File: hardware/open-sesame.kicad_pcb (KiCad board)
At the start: 2 copper layers, 72 x 45 mm, 33 parts, among them J1 Conn_01x02, J2 Conn_01x06, J3 Conn_01x02, J4 Conn_01x02, J5 Conn_01x02, J6 Conn_01x02, J7 Qwiic_RA, U1 CPC1019N, U2 CPC1019N, U3 CPC1019N

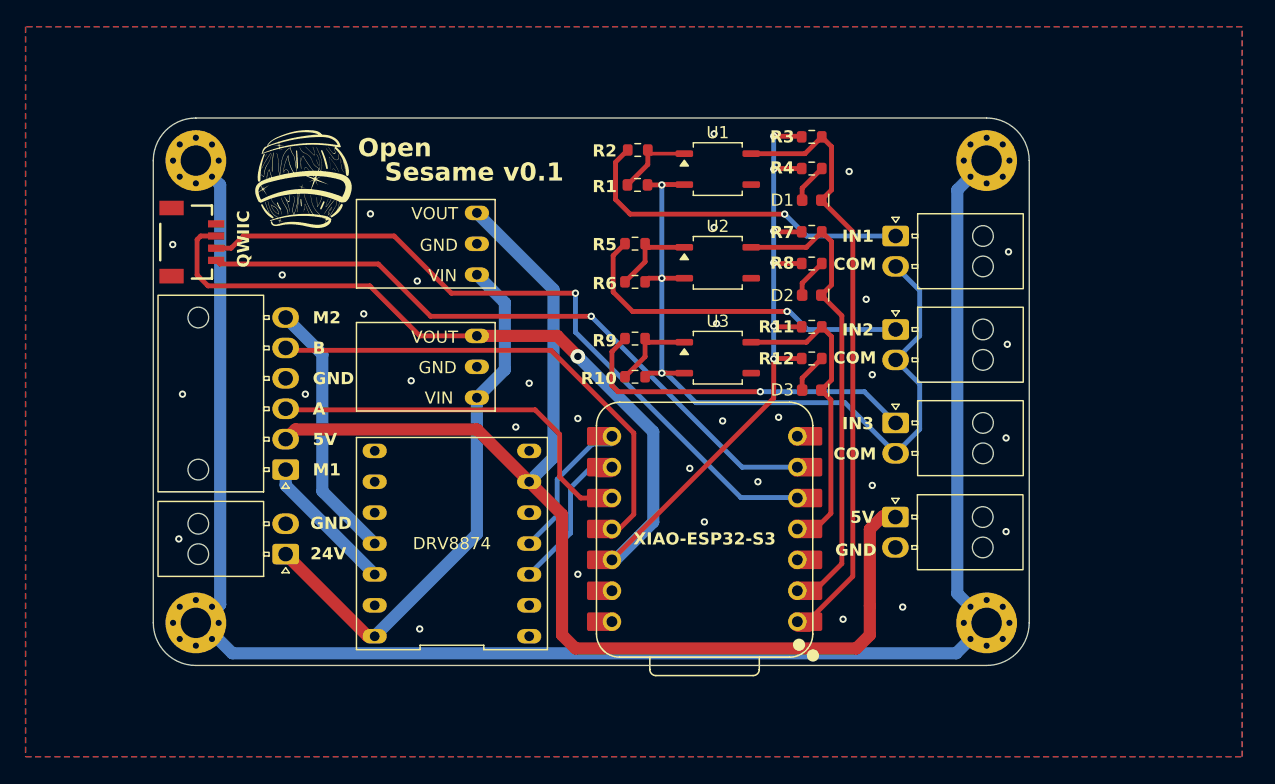
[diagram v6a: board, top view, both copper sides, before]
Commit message: hardware: Use screw connectors and PC817
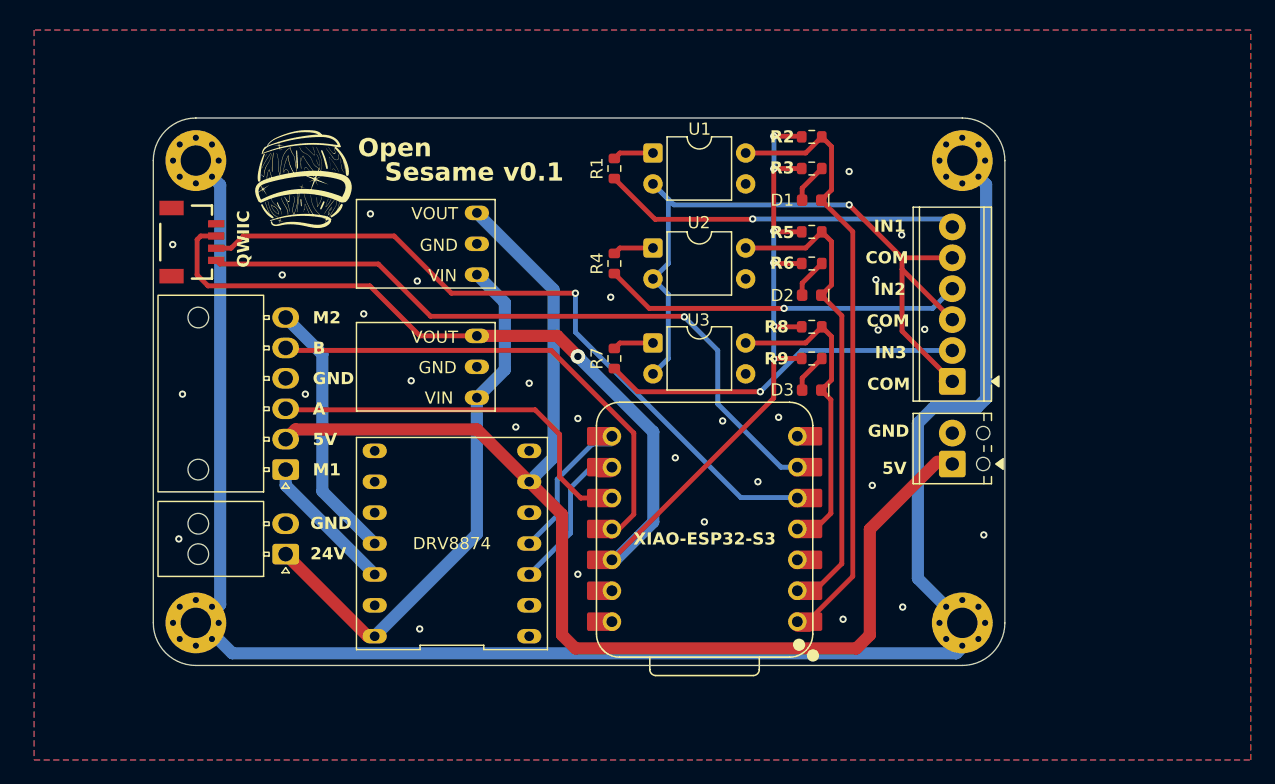
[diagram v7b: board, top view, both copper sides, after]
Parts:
- removed J5, J6: Conn_01x02, Connector_Molex:Molex_Nano-Fit_105313-xx02_1x02_P2.50mm_Horizontal
- removed R10: 750R, Resistor_SMD:R_0603_1608Metric
- removed the R2 at (160.3, 70.1)
- removed the R5 at (160.1, 77.8)
- removed the R6 at (160.1, 81.0)
- removed the R9 at (160.1, 85.6)
- added R4: 330R, Resistor_SMD:R_0603_1608Metric, F.Cu at (158.4, 79.5)
- added R7: 330R, Resistor_SMD:R_0603_1608Metric, F.Cu at (158.4, 87.3)
- J3: value Conn_01x02 -> Screw_Terminal_01x02; footprint Connector_Molex:Molex_Nano-Fit_105313-xx02_1x02_P2.50mm_Horizontal -> TerminalBlock_Phoenix:TerminalBlock_Phoenix_MPT-0,5-2-2.54_1x02_P2.54mm_Horizontal
- J4: value Conn_01x02 -> Screw_Terminal_01x06; footprint Connector_Molex:Molex_Nano-Fit_105313-xx02_1x02_P2.50mm_Horizontal -> TerminalBlock_Phoenix:TerminalBlock_Phoenix_MPT-0,5-6-2.54_1x06_P2.54mm_Horizontal
- R1: value 750R -> 330R
- U1, U2, U3: value CPC1019N -> PC817; footprint Package_SO:SOP-4_3.8x4.1mm_P2.54mm -> Package_DIP:DIP-4_W7.62mm
- moved J4 12.8 mm to (186.2, 89.2), turned to 90 degrees
- moved J3 6.40 mm to (186.2, 95.9), turned to 90 degrees
- moved U1 5.49 mm to (161.6, 70.4)
- moved U2 5.46 mm to (161.6, 78.2)
- moved U3 5.46 mm to (161.6, 86.0)
- moved R1 2.33 mm to (158.4, 71.7), turned to 90 degrees
- moved H1 2.00 mm to (187.0, 71.0)
- moved H2 2.00 mm to (187.0, 109.0)
- renumbered R3 to R2, R4 to R3, R7 to R5, R8 to R6, R11 to R8, R12 to R9
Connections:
- J4 pad 1: IN1 -> IN_COMMON
- J4 pad 2: IN_COMMON -> IN3
- R1 pad 1: Net-(R1-Pad1) -> IN1
- R1 pad 2: IN_COMMON -> Net-(R1-Pad2)
- U1 pad 1: Net-(R1-Pad1) -> Net-(R1-Pad2)
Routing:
- net Net-(R1-Pad1): track 6.69 -> 0.00 mm
- net +5V: track 98.9 -> 104.2 mm
- net Earth: track 146.0 -> 150.8 mm
- net Net-(R7-Pad2): track 7.17 -> 3.36 mm
- net Net-(R4-Pad2): track 7.17 -> 3.36 mm
- net Net-(R1-Pad2): track 0.00 -> 3.36 mm
- net SCL: track 54.8 -> 57.4 mm
- net IN_COMMON: track 65.8 -> 63.5 mm, vias 3 -> 1
- net IN3: track 28.9 -> 30.0 mm
- net IN2: track 28.9 -> 29.6 mm
- net IN1: track 28.7 -> 29.5 mm
- net GND: vias 32 -> 29
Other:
- board size 72 x 45 mm -> 70 x 45 mm

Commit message: hardware: use one power converter, shrink size, change connectors
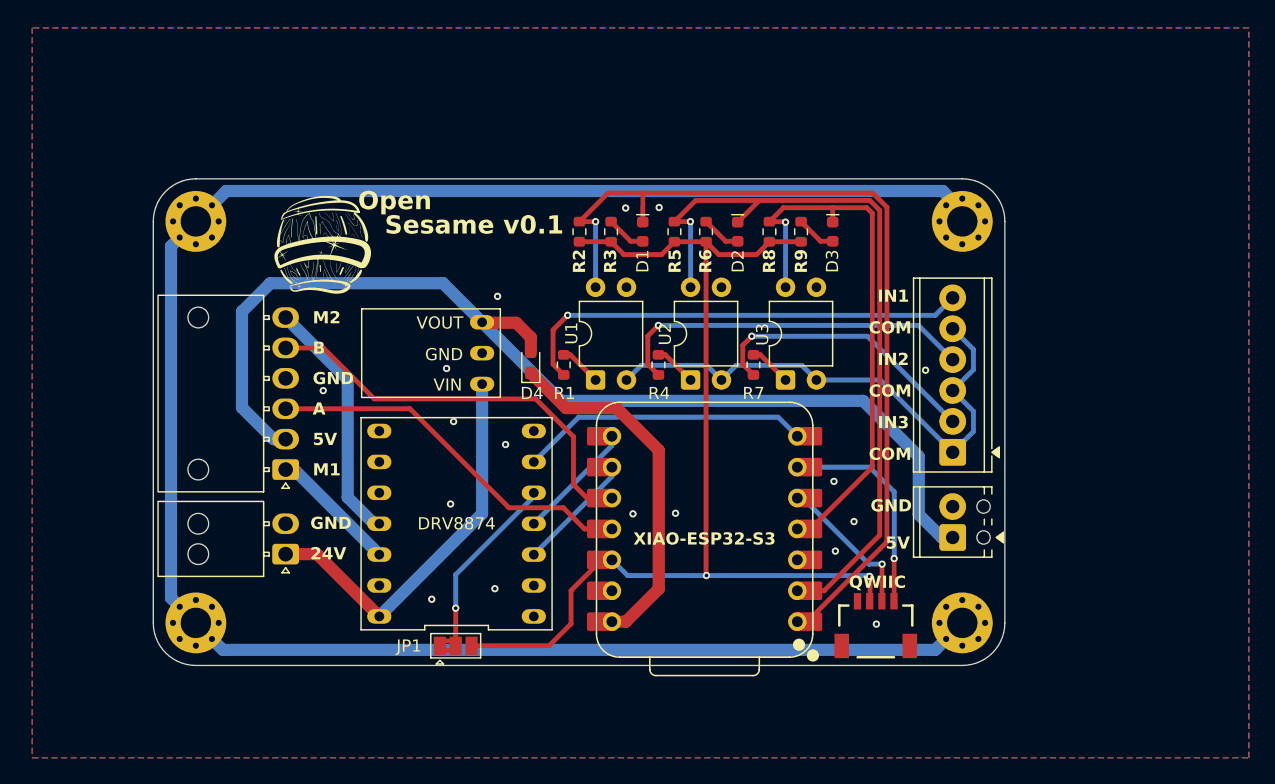
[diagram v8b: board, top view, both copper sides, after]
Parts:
- removed D45V5F2: D45V5F3, MyLibrary:D45V5Fx
- added D4: D_Schottky, Diode_SMD:D_0603_1608Metric_Pad1.05x0.95mm_HandSolder, F.Cu at (151.5, 87.6)
- added JP1: SolderJumper_3_Bridged12, Jumper:SolderJumper-3_P1.3mm_Bridged2Bar12_Pad1.0x1.5mm, F.Cu at (145.4, 110.9)
- moved J7 61.7 mm to (179.9, 107.2), turned to 0 degrees
- moved R2 20.6 mm to (155.5, 76.8), turned to 90 degrees
- moved U1 19.2 mm to (156.9, 89.0), turned to 90 degrees
- moved R3 17.3 mm to (158.1, 76.8), turned to 90 degrees
- moved R1 16.7 mm to (154.2, 87.8)
- moved D1 14.1 mm to (160.7, 76.8), turned to -90 degrees
- moved D3 13.1 mm to (176.3, 76.8), turned to -90 degrees
- moved R7 11.4 mm to (169.8, 87.8)
- moved U3 11.3 mm to (172.5, 89.0), turned to 90 degrees
- moved R5 11.3 mm to (163.3, 76.8), turned to 90 degrees
- moved U2 11.3 mm to (164.7, 89.0), turned to 90 degrees
- moved R9 10.5 mm to (173.7, 76.8), turned to 90 degrees
- moved R4 9.09 mm to (162.0, 87.8)
- moved R6 9.07 mm to (165.9, 76.8), turned to 90 degrees
- moved D45V5F1 9.00 mm to (147.5, 86.8)
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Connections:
- DRV8874 pad 5: GND -> Net-(DRV8874-PMODE)
- DRV8874 pad 6: +5V -> SLP
- XIAO-ESP32-S3 pad 10: A -> B
- XIAO-ESP32-S3 pad 11: B -> A
- XIAO-ESP32-S3 pad 14: unconnected-(XIAO-ESP32-S3-VBUS-Pad14) -> Net-(D4-K)
- XIAO-ESP32-S3 pad 7: unconnected-(XIAO-ESP32-S3-GPIO43_D6_TX-Pad7) -> SLP
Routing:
- net SDA: track 59.0 -> 12.3 mm
- net SCL: track 57.4 -> 17.8 mm
- net Net-(D4-K): track 0.00 -> 29.5 mm
- net +3V3: track 114.0 -> 86.5 mm, vias 7 -> 2
- net SLP: track 0.00 -> 23.8 mm
- net GPIO2: track 39.2 -> 61.7 mm, vias 0 -> 1
- net GPIO1: track 51.0 -> 73.5 mm, vias 0 -> 1
- net GPIO4: track 25.6 -> 46.3 mm, vias 0 -> 1
- net IN_COMMON: track 63.5 -> 44.3 mm, vias 1 -> 0
- net Earth: track 150.8 -> 166.0 mm
- net Net-(DRV8874-PMODE): track 0.00 -> 15.2 mm, vias 0 -> 1
- net +5V: track 104.2 -> 89.1 mm
- net +24V: track 45.2 -> 32.4 mm
- net IN1: track 29.5 -> 38.0 mm
- net B: track 40.8 -> 33.4 mm
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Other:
- board size 70 x 45 mm -> 70 x 40 mm
